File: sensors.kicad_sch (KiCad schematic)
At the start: 10 parts, among them U18 MCP9808T-E_MC, U24 PAC1954T-E_4MX

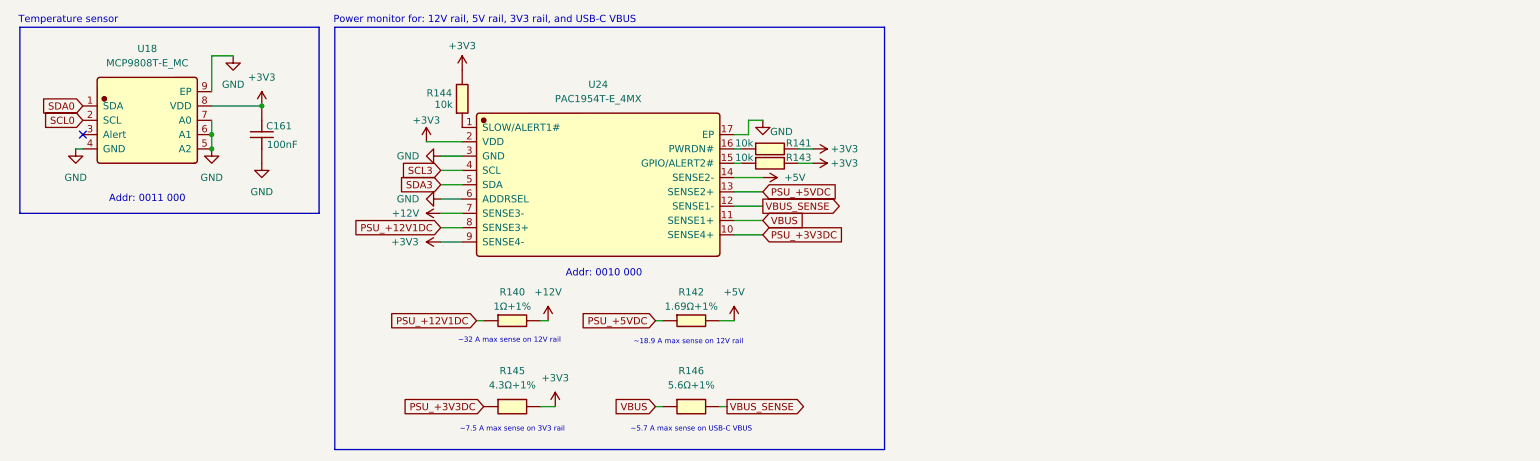
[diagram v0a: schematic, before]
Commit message: Preliminary design of power monitor for PS176, TC358743, LicheeRV nano, and touch display
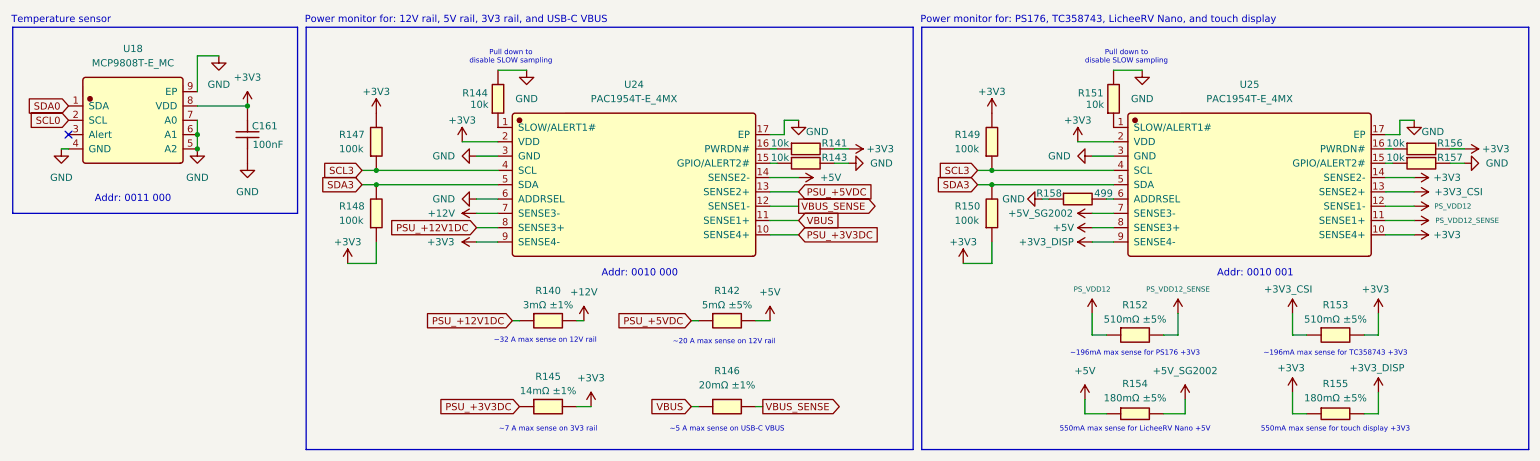
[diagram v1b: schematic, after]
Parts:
- removed R140: 1Ω+1%, Resistor_SMD:R_0402_1005Metric, symbol JLCImport:WR04W1R00FTL
- removed R142: 1.69Ω+1%, Resistor_SMD:R_0402_1005Metric, symbol JLCImport:WR04W1R00FTL
- removed R145: 4.3Ω+1%, Resistor_SMD:R_0402_1005Metric, symbol JLCImport:CL0402FN4R3P
- removed R146: 5.6Ω+1%, Resistor_SMD:R_0402_1005Metric, symbol JLCImport:CL0402FN4R3P
- added R140: 3mΩ ±1%, Resistor_SMD:R_1206_3216Metric, symbol JLCImport:YHR1206SE1WR003F5
- added R142: 5mΩ ±5%, Resistor_SMD:R_1206_3216Metric, symbol JLCImport:YHR1206SE1WR003F5
- added R145: 14mΩ ±1%, Resistor_SMD:R_0805_2012Metric, symbol JLCImport:YHR1206SE1WR003F5
- added R146: 20mΩ ±1%, Resistor_SMD:R_0603_1608Metric, symbol JLCImport:RBL06FTR020
- added R147, R148, R149, R150: 100k, Resistor_SMD:R_0402_1005Metric, symbol JLCImport:0402WGF1003TCE
- added R151, R156, R157: 10k, Resistor_SMD:R_0402_1005Metric, symbol JLCImport:0402WGF1002TCE
- added R152, R153: 510mΩ ±5%, Resistor_SMD:R_1210_3225Metric, symbol JLCImport:YHR1206SE1WR003F5
- added R154, R155: 180mΩ ±5%, Resistor_SMD:R_0508_1220Metric, symbol JLCImport:LTR10EVHJLR18
- added R158: 499, Resistor_SMD:R_0402_1005Metric, symbol JLCImport:WR04W1R00FTL
- added U25: PAC1954T-E_4MX, JLCImport:PAC1954T-E_4MX, symbol JLCImport:PAC1954T-E_4MX
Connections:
- net +12V: now also R140.2
- net +3V3: now also R145.2, R147.2, R148.1, R149.2, R150.1, R153.2, R155.1, R156.2, U25.10 (SENSE4+), U25.14 (SENSE2-), U25.2 (VDD); no longer R143.2, R144.2
- net +5V: now also R142.2, R154.1, U25.8 (SENSE3+)
- net GND: now also R143.2, R144.2, R151.2, R157.2, R158.1, U25.17 (EP), U25.3 (GND)
- net PSU_+12V1DC: now also R140.1
- net PSU_+3V3DC: now also R145.1
- net PSU_+5VDC: now also R142.1
- net SCL3: now also R147.1, R149.1, U25.4 (SCL)
- net SDA3: now also R148.2, R150.2, U25.5 (SDA)
- net VBUS: now also R146.1
- net VBUS_SENSE: now also R146.2
- new net: R151.1, U25.1 (SLOW/ALERT1#)
- new net: R157.1, U25.15 (GPIO/ALERT2#)
- new net: R156.1, U25.16 (PWRDN#)
- new net: R158.2, U25.6 (ADDRSEL)
- new net +3V3_CSI: R153.1, U25.13 (SENSE2+)
- new net +3V3_DISP: R155.2, U25.9 (SENSE4-)
- new net +5V_SG2002: R154.2, U25.7 (SENSE3-)
- new net PS_VDD12: R152.1, U25.12 (SENSE1-)
- new net PS_VDD12_SENSE: R152.2, U25.11 (SENSE1+)
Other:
- note added: "550mA max sense for LicheeRV Nano +5V"
- note added: "550mA max sense for touch display +3V3"
- note added: "Addr: 0010 001"
- note added: "Power monitor for: PS176, TC358743, LicheeRV Nano, and touch display"
- note added: "Pull down to disable SLOW sampling"
- note added: "~196mA max sense for PS176 +3V3"
- note added: "~196mA max sense for TC358743 +3V3"
- note added: "~20 A max sense on 12V rail"
- note added: "~5 A max sense on USB-C VBUS"
- note added: "~7 A max sense on 3V3 rail"
- note removed: "~18.9 A max sense on 12V rail"
- note removed: "~5.7 A max sense on USB-C VBUS"
- note removed: "~7.5 A max sense on 3V3 rail"
- moved on the sheet: C161, R141, R143, R144, U18, U24

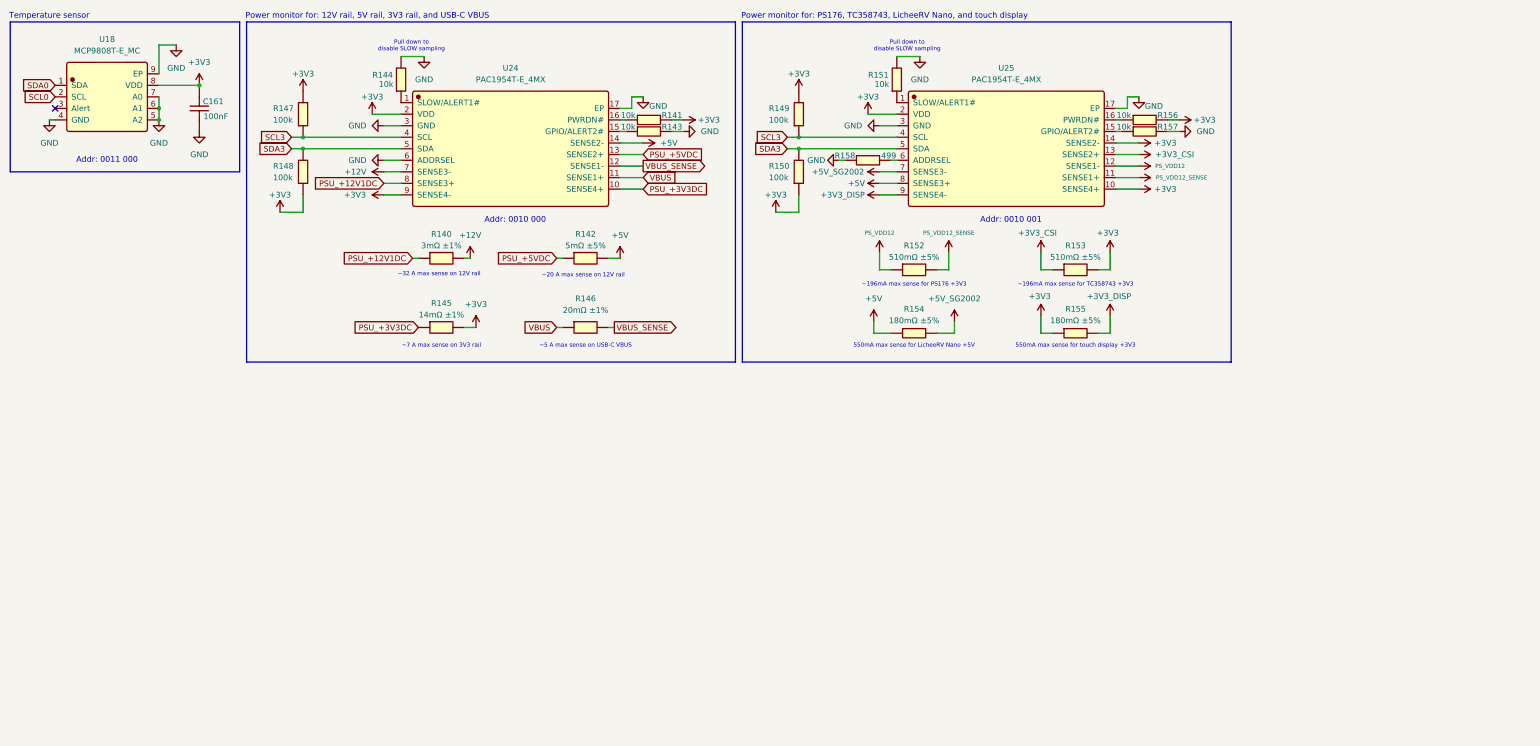
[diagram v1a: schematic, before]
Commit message: Preliminary design of power monitor for USB2244i, 2xRTL9210b + SSD, front panel hub, and 4x chassis fans
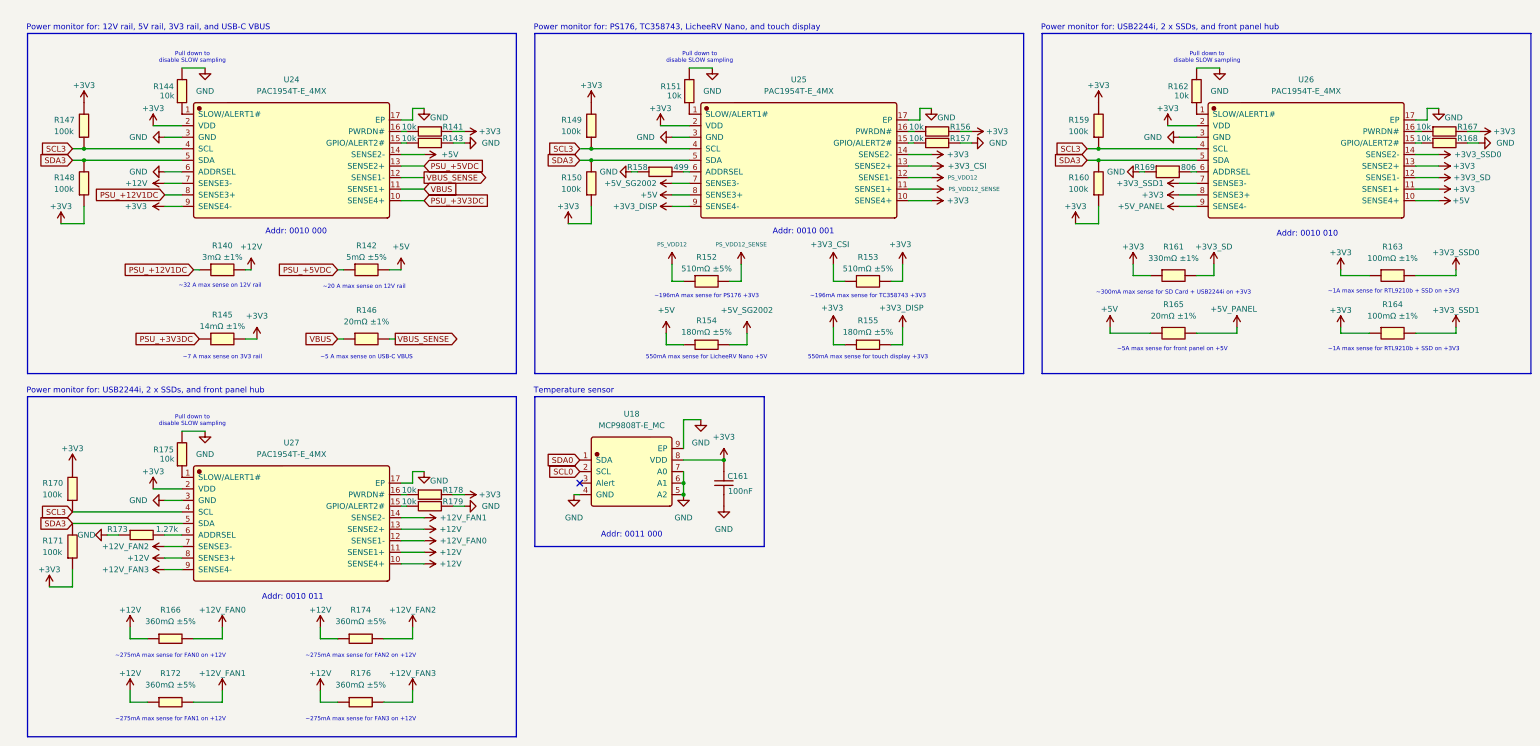
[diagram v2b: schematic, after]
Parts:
- added R159, R160, R170, R171: 100k, Resistor_SMD:R_0402_1005Metric, symbol JLCImport:0402WGF1003TCE
- added R161: 330mΩ ±1%, Resistor_SMD:R_2512_6332Metric, symbol JLCImport:RBJ-12MR330FT
- added R162, R167, R168, R175, R178, R179: 10k, Resistor_SMD:R_0402_1005Metric, symbol JLCImport:0402WGF1002TCE
- added R163, R164: 100mΩ ±1%, Resistor_SMD:R_2512_6332Metric, symbol JLCImport:JER2512F2R100
- added R165: 20mΩ ±1%, Resistor_SMD:R_0603_1608Metric, symbol JLCImport:RBL06FTR020
- added R166, R172, R174, R176: 360mΩ ±5%, Resistor_SMD:R_0805_2012Metric, symbol JLCImport:RTT05R36JTP
- added R169: 806, Resistor_SMD:R_0402_1005Metric, symbol JLCImport:CR0402FF8060G
- added R173: 1.27k, Resistor_SMD:R_0402_1005Metric, symbol JLCImport:WR04X1271FTL
- added U26, U27: PAC1954T-E_4MX, JLCImport:PAC1954T-E_4MX, symbol JLCImport:PAC1954T-E_4MX
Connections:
- net +12V: now also R166.1, R172.1, R174.1, R176.1, U27.10 (SENSE4+), U27.11 (SENSE1+), U27.13 (SENSE2+), U27.8 (SENSE3+)
- net +3V3: now also R159.2, R160.1, R161.1, R163.1, R164.1, R167.2, R170.2, R171.1, R178.2, U26.11 (SENSE1+), U26.13 (SENSE2+), U26.2 (VDD), U26.8 (SENSE3+), U27.2 (VDD)
- net +5V: now also R165.1, U26.10 (SENSE4+)
- net GND: now also R162.2, R168.2, R169.1, R173.1, R175.2, R179.2, U26.17 (EP), U26.3 (GND), U27.17 (EP), U27.3 (GND)
- net SCL3: now also R159.1, R170.1, U26.4 (SCL), U27.4 (SCL)
- net SDA3: now also R160.2, R171.2, U26.5 (SDA), U27.5 (SDA)
- new net: R162.1, U26.1 (SLOW/ALERT1#)
- new net: R179.1, U27.15 (GPIO/ALERT2#)
- new net: R175.1, U27.1 (SLOW/ALERT1#)
- new net: R178.1, U27.16 (PWRDN#)
- new net: R173.2, U27.6 (ADDRSEL)
- new net: R168.1, U26.15 (GPIO/ALERT2#)
- new net: R167.1, U26.16 (PWRDN#)
- new net: R169.2, U26.6 (ADDRSEL)
- new net +12V_FAN0: R166.2, U27.12 (SENSE1-)
- new net +12V_FAN1: R172.2, U27.14 (SENSE2-)
- new net +12V_FAN2: R174.2, U27.7 (SENSE3-)
- new net +12V_FAN3: R176.2, U27.9 (SENSE4-)
- new net +3V3_SD: R161.2, U26.12 (SENSE1-)
- new net +3V3_SSD0: R163.2, U26.14 (SENSE2-)
- new net +3V3_SSD1: R164.2, U26.7 (SENSE3-)
- new net +5V_PANEL: R165.2, U26.9 (SENSE4-)
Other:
- note added: "Addr: 0010 010"
- note added: "Addr: 0010 011"
- note added: "Power monitor for: USB2244i, 2 x SSDs, and front panel hub"
- note added: "~1A max sense for RTL9210b + SSD on +3V3"
- note added: "~275mA max sense for FAN0 on +12V"
- note added: "~275mA max sense for FAN1 on +12V"
- note added: "~275mA max sense for FAN2 on +12V"
- note added: "~275mA max sense for FAN3 on +12V"
- note added: "~300mA max sense for SD Card + USB2244i on +3V3"
- note added: "~5A max sense for front panel on +5V"
- company: (none) -> Designed by: Matthew Kong
- title: (none) -> Temperature and Power monitor sensors
- moved on the sheet: C161, R140, R141, R142, R143, R144, R145, R146, R147, R148, R149, R150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

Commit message: Preliminary design of RTL9210b SSD subsystem
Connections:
- net +3V3_SSD0: no longer R163.2
- net +3V3_SSD1: no longer R164.2
- new net +3V3_SSD0_unfiltered: R163.2
- new net +3V3_SSD1_unfiltered: R164.2
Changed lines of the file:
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@@
 	(wire
 		(pts
-			(xy 332.74 73.66) (xy 323.85 73.66)
+			(xy 336.55 73.66) (xy 323.85 73.66)
 		)
 		(stroke
@@
 	(wire
 		(pts
-			(xy 332.74 86.36) (xy 323.85 86.36)
+			(xy 336.55 86.36) (xy 323.85 86.36)
 		)
 		(stroke
@@
 	(wire
 		(pts
-			(xy 332.74 85.09) (xy 332.74 86.36)
+			(xy 336.55 85.09) (xy 336.55 86.36)
 		)
 		(stroke
@@
 	(wire
 		(pts
-			(xy 332.74 72.39) (xy 332.74 73.66)
+			(xy 336.55 72.39) (xy 336.55 73.66)
 		)
 		(stroke
@@
 	(symbol
 		(lib_id "power:+3V3")
-		(at 332.74 85.09 0)
-		(unit 1)
-		(body_style 1)
-		(exclude_from_sim no)
-		(in_bom yes)
-		(on_board yes)
-		(in_pos_files yes)
-		(dnp no)
-		(property "Reference" "#PWR0359"
-			(at 332.74 88.9 0)
-			(hide yes)
-			(show_name no)
-			(do_not_autoplace no)
-			(effects
-				(font
-					(size 1.27 1.27)
-				)
-			)
-		)
-		(property "Value" "+3V3_SSD1"
-			(at 332.74 81.28 0)
-			(show_name no)
-			(do_not_autoplace no)
-			(effects
-				(font
-					(size 1.27 1.27)
-				)
-			)
-		)
-		(property "Footprint" ""
-			(at 332.74 85.09 0)
-			(hide yes)
-			(show_name no)
-			(do_not_autoplace no)
-			(effects
-				(font
-					(size 1.27 1.27)
-				)
-			)
-		)
-		(property "Datasheet" ""
-			(at 332.74 85.09 0)
-			(hide yes)
-			(show_name no)
-			(do_not_autoplace no)
-			(effects
-				(font
-					(size 1.27 1.27)
-				)
-			)
-		)
-		(property "Description" "Power symbol creates a global label with name \"+3V3\""
-			(at 332.74 85.09 0)
-			(hide yes)
-			(show_name no)
-			(do_not_autoplace no)
-			(effects
-				(font
-					(size 1.27 1.27)
-				)
-			)
-		)
-		(pin "1"
-		)
-		(instances
-			(project "serverv2_backplane"
-				(path "/a90d5657-3125-49af-9845-930d74e449d0"
-					(reference "#PWR0359")
-					(unit 1)
-				)
-			)
-		)
-	)
-	(symbol
-		(lib_id "power:+3V3")
 		(at 195.58 71.12 0)
 		(unit 1)
@@
 	(symbol
 		(lib_id "power:+3V3")
+		(at 336.55 85.09 0)
+		(unit 1)
+		(body_style 1)
+		(exclude_from_sim no)
+		(in_bom yes)
+		(on_board yes)
+		(in_pos_files yes)
+		(dnp no)
+		(property "Reference" "#PWR0359"
+			(at 336.55 88.9 0)
+			(hide yes)
+			(show_name no)
+			(do_not_autoplace no)
+			(effects
+				(font
+					(size 1.27 1.27)
+				)
+			)
+		)
+		(property "Value" "+3V3_SSD1_unfiltered"
+			(at 336.55 81.28 0)
+			(show_name no)
+			(do_not_autoplace no)
+			(effects
+				(font
+					(size 1.27 1.27)
+				)
+			)
+		)
+		(property "Footprint" ""
+			(at 336.55 85.09 0)
+			(hide yes)
+			(show_name no)
+			(do_not_autoplace no)
+			(effects
+				(font
+					(size 1.27 1.27)
+				)
+			)
+		)
+		(property "Datasheet" ""
+			(at 336.55 85.09 0)
+			(hide yes)
+			(show_name no)
+			(do_not_autoplace no)
+			(effects
+				(font
+					(size 1.27 1.27)
+				)
+			)
+		)
+		(property "Description" "Power symbol creates a global label with name \"+3V3\""
+			(at 336.55 85.09 0)
+			(hide yes)
+			(show_name no)
+			(do_not_autoplace no)
+			(effects
+				(font
+					(size 1.27 1.27)
+				)
+			)
+		)
+		(pin "1"
+		)
+		(instances
+			(project "serverv2_backplane"
+				(path "/a90d5657-3125-49af-9845-930d74e449d0"
+					(reference "#PWR0359")
+					(unit 1)
+				)
+			)
+		)
+	)
+	(symbol
+		(lib_id "power:+3V3")
 		(at 48.26 138.43 90)
 		(unit 1)
@@
 	(symbol
 		(lib_id "power:+3V3")
-		(at 332.74 72.39 0)
+		(at 336.55 72.39 0)
 		(unit 1)
 		(body_style 1)
@@
 		(dnp no)
 		(property "Reference" "#PWR0357"
-			(at 332.74 76.2 0)
+			(at 336.55 76.2 0)
 			(hide yes)
 			(show_name no)
@@
 			)
 		)
-		(property "Value" "+3V3_SSD0"
-			(at 332.74 68.58 0)
+		(property "Value" "+3V3_SSD0_unfiltered"
+			(at 336.55 68.58 0)
 			(show_name no)
 			(do_not_autoplace no)
@@
 		)
 		(property "Footprint" ""
-			(at 332.74 72.39 0)
+			(at 336.55 72.39 0)
 			(hide yes)
 			(show_name no)
@@
 		)
 		(property "Datasheet" ""
-			(at 332.74 72.39 0)
+			(at 336.55 72.39 0)
 			(hide yes)
 			(show_name no)
@@
 		)
 		(property "Description" "Power symbol creates a global label with name \"+3V3\""
-			(at 332.74 72.39 0)
+			(at 336.55 72.39 0)
 			(hide yes)
 			(show_name no)
